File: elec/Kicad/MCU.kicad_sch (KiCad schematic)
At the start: 13 parts, among them U1 STM32L053C8T6, Y1 32MHz

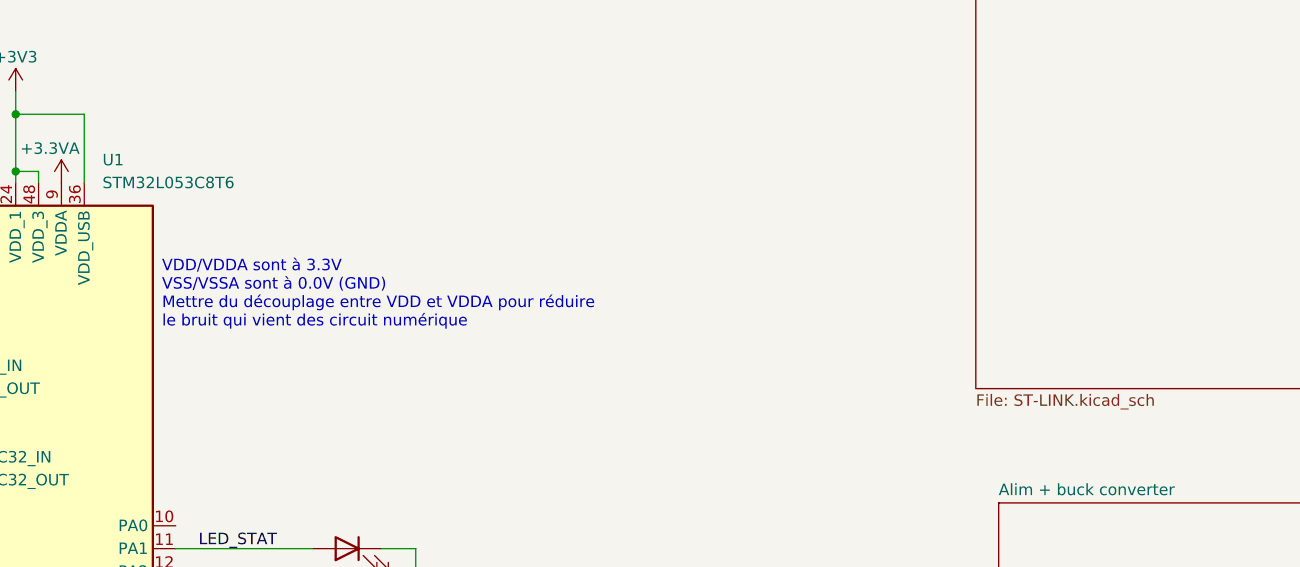
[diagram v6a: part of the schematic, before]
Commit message: start the battery managemennt
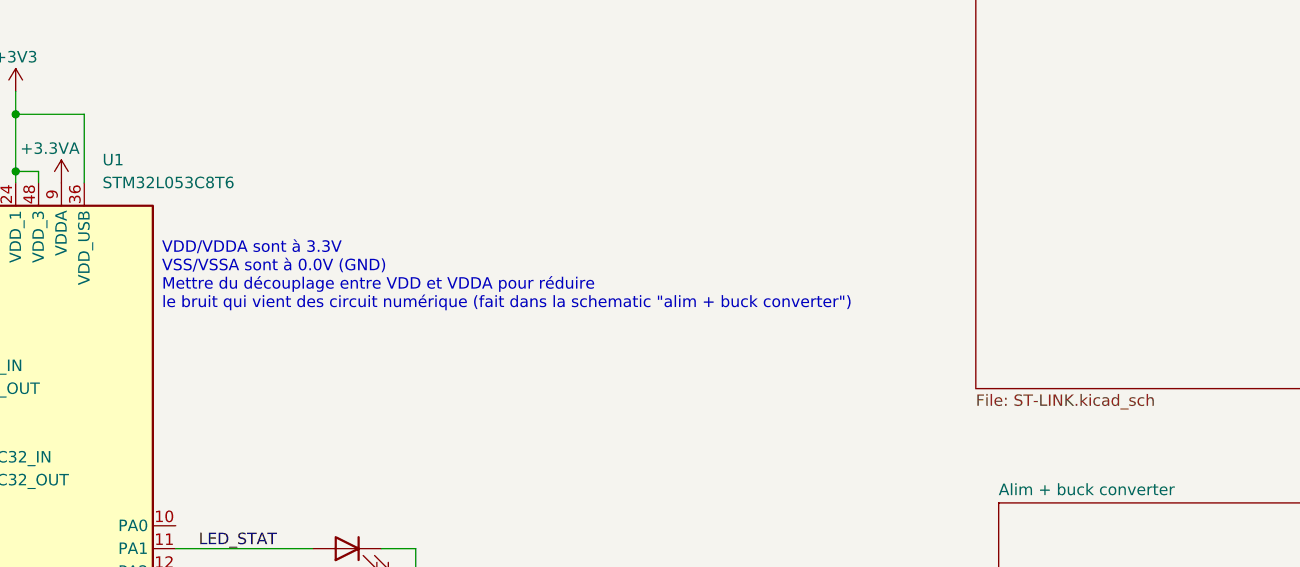
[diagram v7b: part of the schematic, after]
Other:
- note added: "VDD/VDDA sont à 3.3V VSS/VSSA sont à 0.0V (GND) Mettre du découplage entre VDD et VDDA pour réduire le bruit qui vient des circuit numérique (fait dans la schematic "alim + buck converter")"
- note removed: "VDD/VDDA sont à 3.3V VSS/VSSA sont à 0.0V (GND) Mettre du découplage entre VDD et VDDA pour réduire le bruit qui vient des circuit numérique"
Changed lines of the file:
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@@
 		)
 	)
-	(text "VDD/VDDA sont à 3.3V\nVSS/VSSA sont à 0.0V (GND)\nMettre du découplage entre VDD et VDDA pour réduire \nle bruit qui vient des circuit numérique\n\n"
+	(text "VDD/VDDA sont à 3.3V\nVSS/VSSA sont à 0.0V (GND)\nMettre du découplage entre VDD et VDDA pour réduire \nle bruit qui vient des circuit numérique (fait dans la schematic \"alim + buck converter\")\n\n\n"
 		(exclude_from_sim no)
 		(at 111.506 79.248 0)

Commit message: sa progresse. Battery management fini + humidity/temp sensor + bouton
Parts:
- added R19, R20: 4K7, symbol Device:R
- D2: value GREEN -> BLUE
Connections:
- net +3V3: now also R19.1, R20.1
- net PH0: now also U1.6 (PH1/OSC_OUT)
- net PH1: now also U1.5 (PH0/OSC_IN)
- net ADC_IN2: now reaches U1.12 (PA2)
- net ADC_IN3: now reaches U1.13 (PA3)
- net SPI1_SCK: now reaches U1.15 (PA5)
- net SPI1_MISO: now reaches U1.16 (PA6)
- net SPI1_MOSI: now reaches U1.17 (PA7)
- net PB2_Bouton_LOG: now reaches U1.20 (PB2)
- net PB10_Bouton_BACK: now reaches U1.21 (PB10)
- net PB11_Bouton_IN: now reaches U1.22 (PB11)
- net CS_SD: now reaches U1.25 (PB12)
- net I2C1_SCL: now reaches U1.45 (PB8)
- net I2C1_SCL: now also R19.2
- net I2C1_SDA: now reaches U1.46 (PB9)
- net I2C1_SDA: now also R20.2
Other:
- note added: "Notes: - Le débogeur du STM32L0538-DISCO est le STMF103CBT6 - On veux avoir les led suivante: 1. LED qui indique que la batterie charge (soit que le 5V est branché) = fait (LED rouge) 2. LED quand on est en bootmode 3. LED qui indique que c'est la batterie qui est utilisé comme alim - Vérifier le courant/Tension qui passe dans les DELs si c'est chill - Diviseur de tension pour la batterie afin de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"
- note added: "OSC_IN/OSC_OUT (pour le HSE = High-Speed external crystal, soit le crystal principal) OSC32_IN/OSC32_OUT (pour le LSE = Low-Speed external crystal, soit le crystal secondaire)"
- note removed: "Notes: - Le débogeur du STM32L0538-DISCO est le STMF103CBT6 - On veux avoir les led suivante: 1. LED qui indique que la batterie charge (soit que le 5V est branché) 2. LED quand on est en bootmode 3. LED qui indique que c'est la batterie qui est utilisé comme alim"
